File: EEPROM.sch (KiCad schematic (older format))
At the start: 22 parts, among them IC1 PCA6408APW, IC2 AT24CS01, U2 TPS613221ADBVT

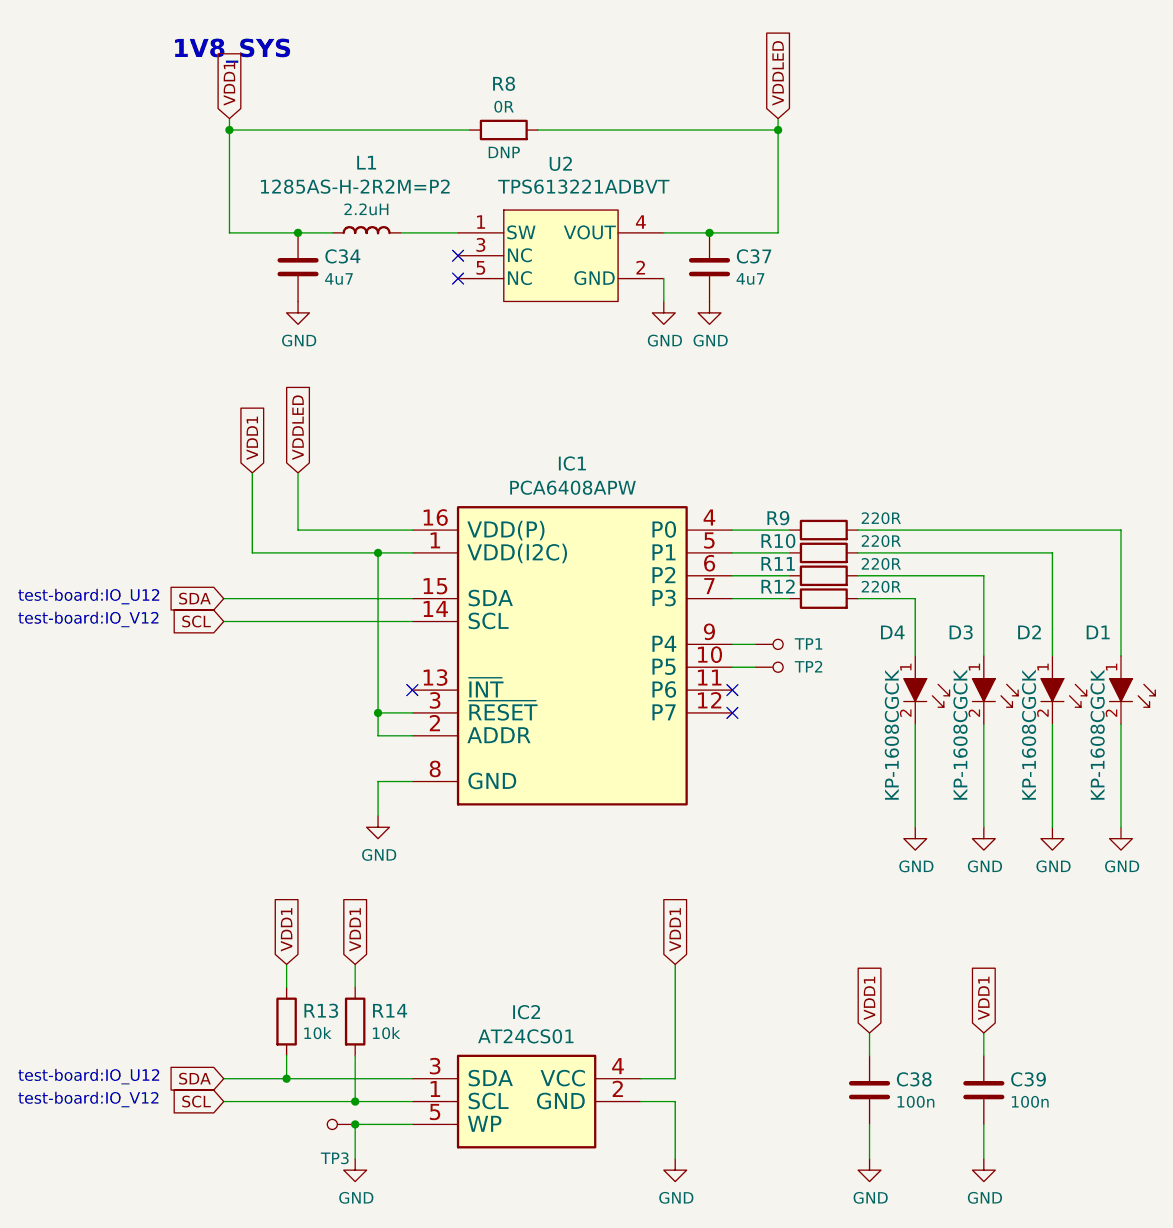
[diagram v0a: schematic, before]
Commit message: Fix power labels naming scheme, remove connection from SODIM to VDDQ, add chockes to DDR5 power
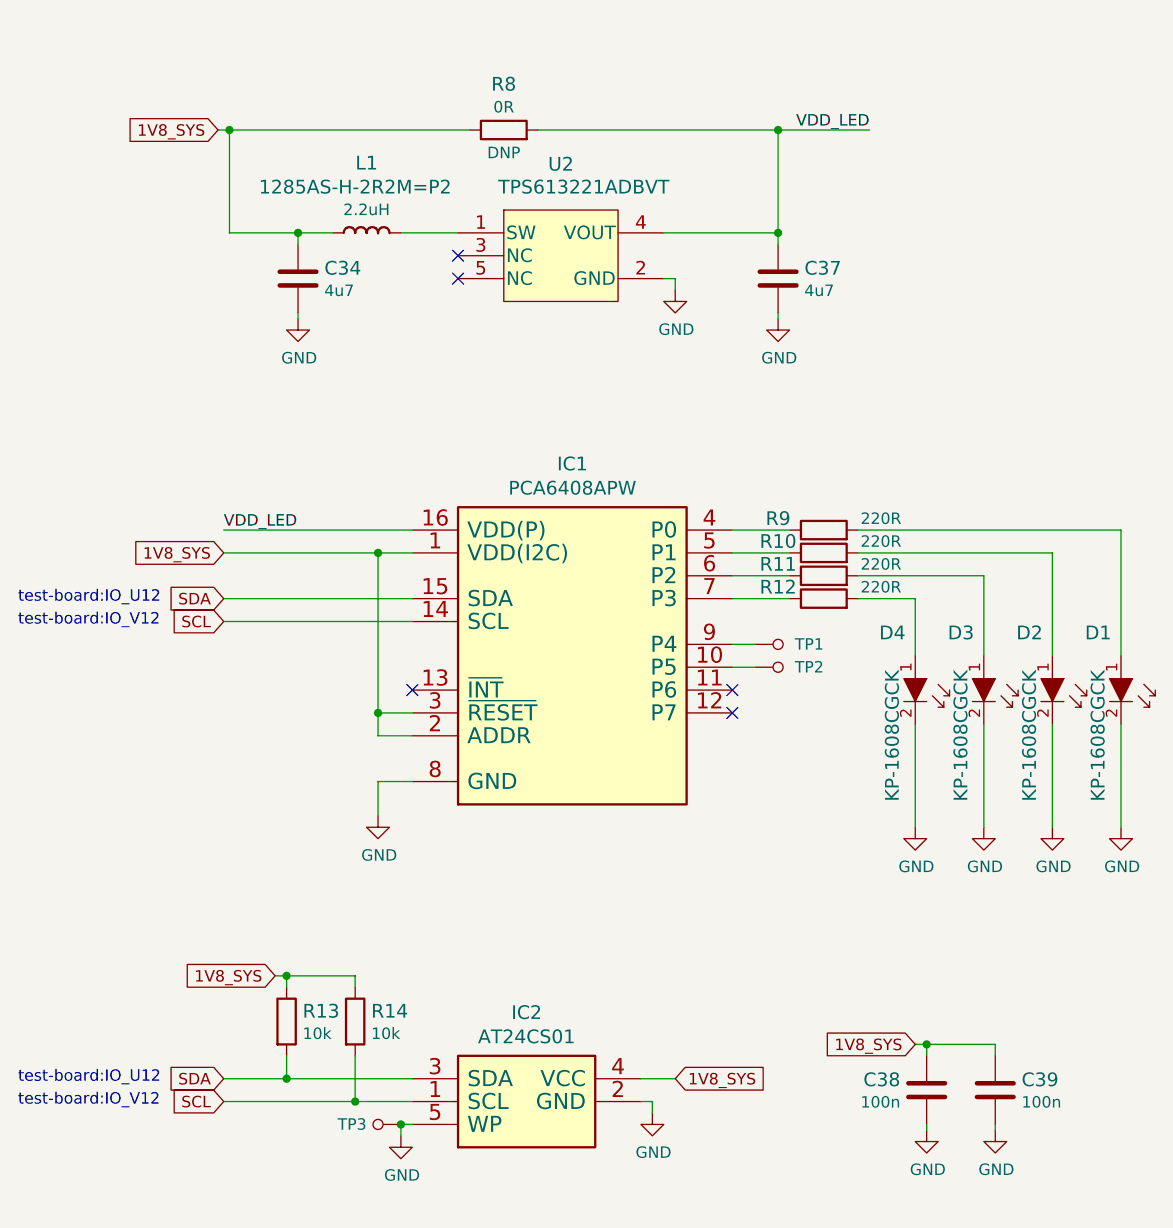
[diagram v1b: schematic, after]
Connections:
- net VDD1 renamed 1V8_SYS
- net VDDLED renamed VDD_LED
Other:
- note removed: "1V8_SYS"
- moved on the sheet: C34, C37, C38, C39, TP3
